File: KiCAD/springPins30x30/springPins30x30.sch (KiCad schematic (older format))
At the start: 20 parts, among them P1 CONN_02X03, P2 CONN_02X03, P3 CONN_02X03, P4 CONN_02X03

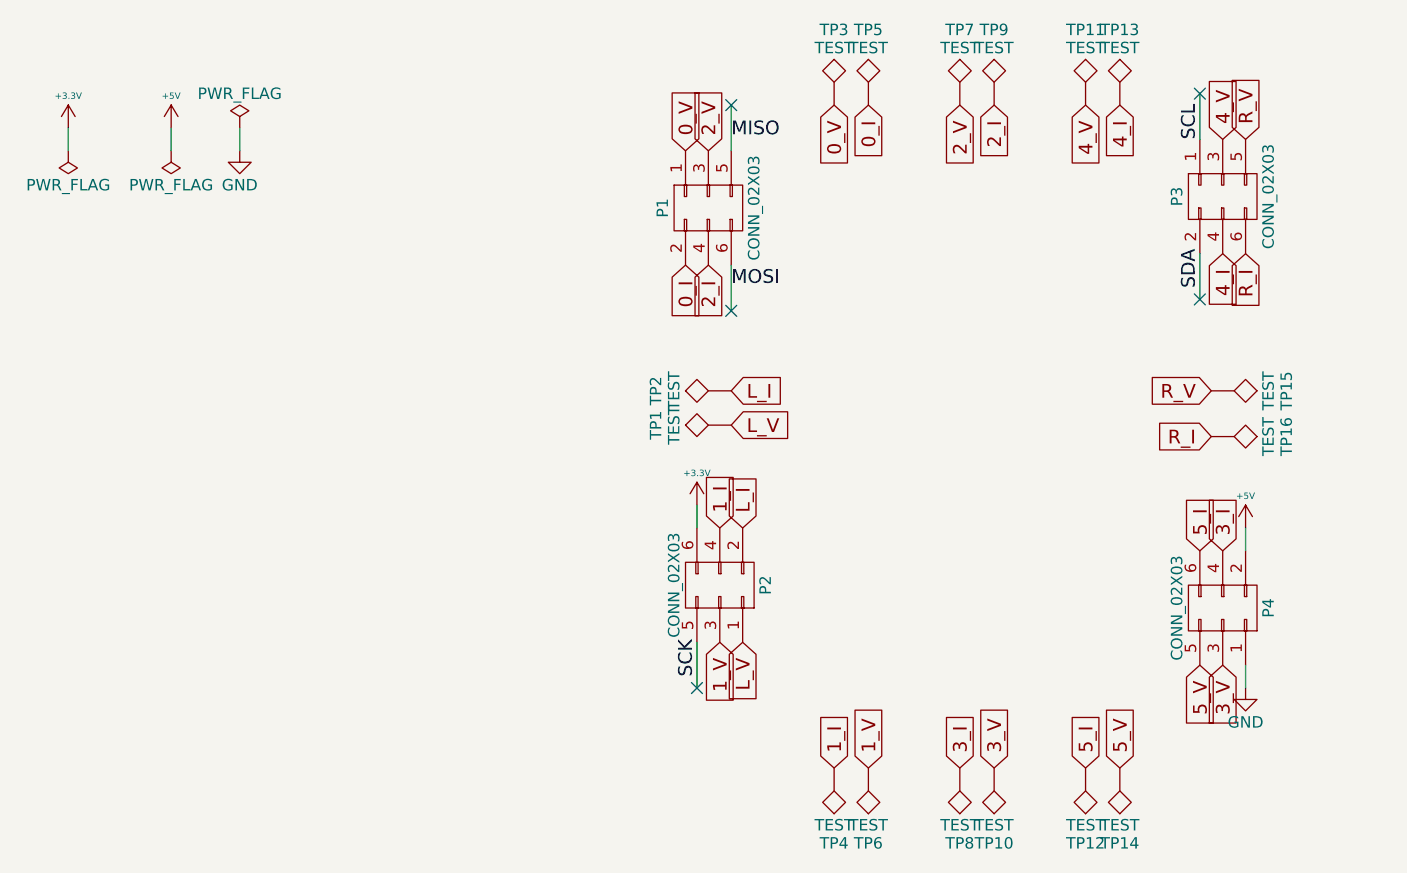
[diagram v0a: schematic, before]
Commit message: fix pwr/gnd swap, fix extra clock signal name, fix pin hole sizes
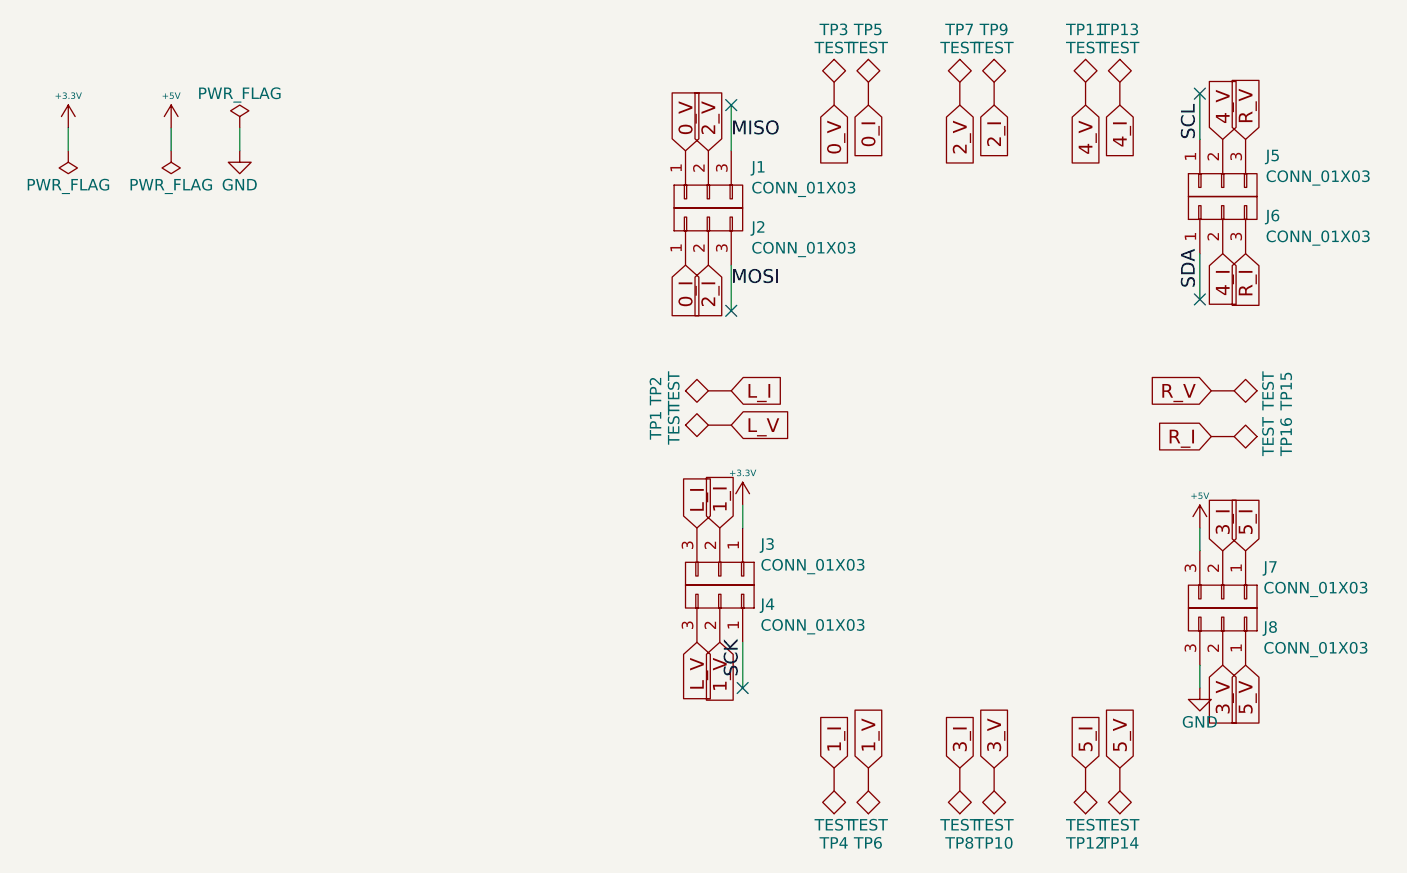
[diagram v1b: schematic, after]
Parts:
- removed P1, P2, P3, P4: CONN_02X03, myParts:RSM-103-02-L-D, symbol CONN_02X03
- added J1, J2, J3, J4, J5, J6, J7, J8: CONN_01X03, myParts:M50-3130342, symbol CONN_01X03
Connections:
- net +3V3: now also J3.1 (P1)
- net +5V: now also J7.3 (P3)
- net 0_I: now also J2.1 (P1)
- net 0_V: now also J1.1 (P1)
- net 1_I: now also J3.2 (P2)
- net 1_V: now also J4.2 (P2)
- net 2_I: now also J2.2 (P2)
- net 2_V: now also J1.2 (P2)
- net 3_I: now also J7.2 (P2)
- net 3_V: now also J8.2 (P2)
- net 4_I: now also J6.2 (P2)
- net 4_V: now also J5.2 (P2)
- net 5_I: now also J7.1 (P1)
- net 5_V: now also J8.1 (P1)
- net GND: now also J8.3 (P3)
- net L_I: now also J3.3 (P3)
- net L_V: now also J4.3 (P3)
- net MISO: now also J1.3 (P3)
- net MOSI: now also J2.3 (P3)
- net R_I: now also J6.3 (P3)
- net R_V: now also J5.3 (P3)
- net SCK: now also J4.1 (P1)
- net SCL: now also J5.1 (P1)
- net SDA: now also J6.1 (P1)
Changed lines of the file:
@@
 LIBS:contrib
 LIBS:valves
-LIBS:spingPins30x30-cache
-EELAYER 25 0
+LIBS:springPins30x30-cache
+EELAYER 26 0
 EELAYER END
 $Descr A4 11693 8268
@@
 	0    1    -1   0
 $EndComp
-Text GLabel 4050 4750 3    60   Input ~ 0
+Text GLabel 3850 4750 3    60   Input ~ 0
 L_V
 Text GLabel 6250 2550 1    60   Input ~ 0
@@
 Text GLabel 6150 4350 1    60   Input ~ 0
 3_I
-Text GLabel 6050 4350 1    60   Input ~ 0
+Text GLabel 6250 4350 1    60   Input ~ 0
 5_I
 Text GLabel 3800 2600 1    60   Input ~ 0
@@
 Text GLabel 6150 4850 3    60   Input ~ 0
 3_V
-Text GLabel 6050 4850 3    60   Input ~ 0
+Text GLabel 6250 4850 3    60   Input ~ 0
 5_V
 $Comp
 L GND #PWR01
 U 1 1 58E4DB9E
-P 6250 4950
-F 0 "#PWR01" H 6250 4700 50  0001 C CNN
-F 1 "GND" H 6250 4800 50  0000 C CNN
-F 2 "" H 6250 4950 50  0000 C CNN
-F 3 "" H 6250 4950 50  0000 C CNN
-	1    6250 4950
-	-1   0    0    -1
+P 6050 4950
+F 0 "#PWR01" H 6050 4700 50  0001 C CNN
+F 1 "GND" H 6050 4800 50  0000 C CNN
+F 2 "" H 6050 4950 50  0000 C CNN
+F 3 "" H 6050 4950 50  0000 C CNN
+	1    6050 4950
+	1    0    0    -1
 $EndComp
 $Comp
 L +3.3V #PWR02
 U 1 1 58E4DBA4
-P 3850 4150
-F 0 "#PWR02" H 3850 4000 50  0001 C CNN
-F 1 "+3.3V" H 3850 4290 28  0000 C CNN
-F 2 "" H 3850 4150 50  0000 C CNN
-F 3 "" H 3850 4150 50  0000 C CNN
-	1    3850 4150
-	1    0    0    -1
+P 4050 4150
+F 0 "#PWR02" H 4050 4000 50  0001 C CNN
+F 1 "+3.3V" H 4050 4290 28  0000 C CNN
+F 2 "" H 4050 4150 50  0000 C CNN
+F 3 "" H 4050 4150 50  0000 C CNN
+	1    4050 4150
+	-1   0    0    -1
 $EndComp
 $Comp
 L +5V #PWR03
 U 1 1 58E4DBAA
-P 6250 4250
-F 0 "#PWR03" H 6250 4100 50  0001 C CNN
-F 1 "+5V" H 6250 4390 28  0000 C CNN
-F 2 "" H 6250 4250 50  0000 C CNN
-F 3 "" H 6250 4250 50  0000 C CNN
-	1    6250 4250
-	-1   0    0    -1
-$EndComp
-$Comp
-L CONN_02X03 P1
-U 1 1 58E4DBB6
-P 3900 2850
-F 0 "P1" H 3900 3050 50  0000 C CNN
-F 1 "CONN_02X03" H 3900 2650 50  0000 C CNN
-F 2 "myParts:RSM-103-02-L-D" H 3900 1650 50  0001 C CNN
-F 3 "" H 3900 1650 50  0000 C CNN
-	1    3900 2850
-	0    -1   1    0
-$EndComp
-$Comp
-L CONN_02X03 P3
-U 1 1 58E4DBBD
-P 6150 2800
-F 0 "P3" H 6150 3000 50  0000 C CNN
-F 1 "CONN_02X03" H 6150 2600 50  0000 C CNN
-F 2 "myParts:RSM-103-02-L-D" H 6150 1600 50  0001 C CNN
-F 3 "" H 6150 1600 50  0000 C CNN
-	1    6150 2800
-	0    -1   1    0
-$EndComp
-$Comp
-L CONN_02X03 P2
-U 1 1 58E4DBC4
-P 3950 4500
-F 0 "P2" H 3950 4700 50  0000 C CNN
-F 1 "CONN_02X03" H 3950 4300 50  0000 C CNN
-F 2 "myParts:RSM-103-02-L-D" H 3950 3300 50  0001 C CNN
-F 3 "" H 3950 3300 50  0000 C CNN
-	1    3950 4500
-	0    1    -1   0
-$EndComp
-$Comp
-L CONN_02X03 P4
-U 1 1 58E4DBCB
-P 6150 4600
-F 0 "P4" H 6150 4800 50  0000 C CNN
-F 1 "CONN_02X03" H 6150 4400 50  0000 C CNN
-F 2 "myParts:RSM-103-02-L-D" H 6150 3400 50  0001 C CNN
-F 3 "" H 6150 3400 50  0000 C CNN
-	1    6150 4600
-	0    1    -1   0
-$EndComp
-Text GLabel 4050 4250 1    60   Input ~ 0
+P 6050 4250
+F 0 "#PWR03" H 6050 4100 50  0001 C CNN
+F 1 "+5V" H 6050 4390 28  0000 C CNN
+F 2 "" H 6050 4250 50  0000 C CNN
+F 3 "" H 6050 4250 50  0000 C CNN
+	1    6050 4250
+	1    0    0    -1
+$EndComp
+Text GLabel 3850 4250 1    60   Input ~ 0
 L_I
 Wire Wire Line
-	3850 4150 3850 4250
-Wire Wire Line
-	6250 4250 6250 4350
-Wire Wire Line
-	6250 4850 6250 4950
+	4050 4150 4050 4250
+Wire Wire Line
+	6050 4250 6050 4350
+Wire Wire Line
+	6050 4850 6050 4950
 Text GLabel 4450 2400 3    60   Input ~ 0
 0_V
@@
 SDA
 Wire Wire Line
-	3850 4750 3850 4950
-Text Label 3850 4900 1    60   ~ 0
+	4050 4750 4050 4950
+Text Label 4050 4900 1    60   ~ 0
 SCK
-NoConn ~ 3850 4950
+NoConn ~ 4050 4950
 $Comp
 L PWR_FLAG #FLG04
@@
 Wire Wire Line
 	1850 2500 1850 2600
+$Comp
+L CONN_01X03 J1
+U 1 1 592420F2
+P 3900 2800
+F 0 "J1" V 3772 2612 50  0000 R CNN
+F 1 "CONN_01X03" V 3863 2612 50  0000 R CNN
+F 2 "myParts:M50-3130342" H 3900 2800 50  0001 C CNN
+F 3 "" H 3900 2800 50  0001 C CNN
+	1    3900 2800
+	0    -1   1    0
+$EndComp
+$Comp
+L CONN_01X03 J5
+U 1 1 59242209
+P 6150 2750
+F 0 "J5" V 6022 2562 50  0000 R CNN
+F 1 "CONN_01X03" V 6113 2562 50  0000 R CNN
+F 2 "myParts:M50-3130342" H 6150 2750 50  0001 C CNN
+F 3 "" H 6150 2750 50  0001 C CNN
+	1    6150 2750
+	0    -1   1    0
+$EndComp
+$Comp
+L CONN_01X03 J4
+U 1 1 592422A3
+P 3950 4550
+F 0 "J4" V 3915 4728 50  0000 L CNN
+F 1 "CONN_01X03" V 3824 4728 50  0000 L CNN
+F 2 "myParts:M50-3130342" H 3950 4550 50  0001 C CNN
+F 3 "" H 3950 4550 50  0001 C CNN
+	1    3950 4550
+	0    1    -1   0
+$EndComp
+$Comp
+L CONN_01X03 J8
+U 1 1 592423C0
+P 6150 4650
+F 0 "J8" V 6115 4828 50  0000 L CNN
+F 1 "CONN_01X03" V 6024 4828 50  0000 L CNN
+F 2 "myParts:M50-3130342" H 6150 4650 50  0001 C CNN
+F 3 "" H 6150 4650 50  0001 C CNN
+	1    6150 4650
+	0    1    -1   0
+$EndComp
+$Comp
+L CONN_01X03 J2
+U 1 1 5924241A
+P 3900 2900
+F 0 "J2" V 3865 2712 50  0000 R CNN
+F 1 "CONN_01X03" V 3774 2712 50  0000 R CNN
+F 2 "myParts:M50-3130342" H 3900 2900 50  0001 C CNN
+F 3 "" H 3900 2900 50  0001 C CNN
+	1    3900 2900
+	0    -1   -1   0
+$EndComp
+$Comp
+L CONN_01X03 J6
+U 1 1 592424B8
+P 6150 2850
+F 0 "J6" V 6115 2662 50  0000 R CNN
+F 1 "CONN_01X03" V 6024 2662 50  0000 R CNN
+F 2 "myParts:M50-3130342" H 6150 2850 50  0001 C CNN
+F 3 "" H 6150 2850 50  0001 C CNN
+	1    6150 2850
+	0    -1   -1   0
+$EndComp
+$Comp
+L CONN_01X03 J3
+U 1 1 59242522
+P 3950 4450
+F 0 "J3" V 3822 4628 50  0000 L CNN
+F 1 "CONN_01X03" V 3913 4628 50  0000 L CNN
+F 2 "myParts:M50-3130342" H 3950 4450 50  0001 C CNN
+F 3 "" H 3950 4450 50  0001 C CNN
+	1    3950 4450
+	0    1    1    0
+$EndComp
+$Comp
+L CONN_01X03 J7
+U 1 1 5924258A
+P 6150 4550
+F 0 "J7" V 6022 4728 50  0000 L CNN
+F 1 "CONN_01X03" V 6113 4728 50  0000 L CNN
+F 2 "myParts:M50-3130342" H 6150 4550 50  0001 C CNN
+F 3 "" H 6150 4550 50  0001 C CNN
+	1    6150 4550
+	0    1    1    0
+$EndComp
 $EndSCHEMATC
